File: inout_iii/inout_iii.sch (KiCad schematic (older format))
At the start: 1 part, among them P1 DIN_41612_128P

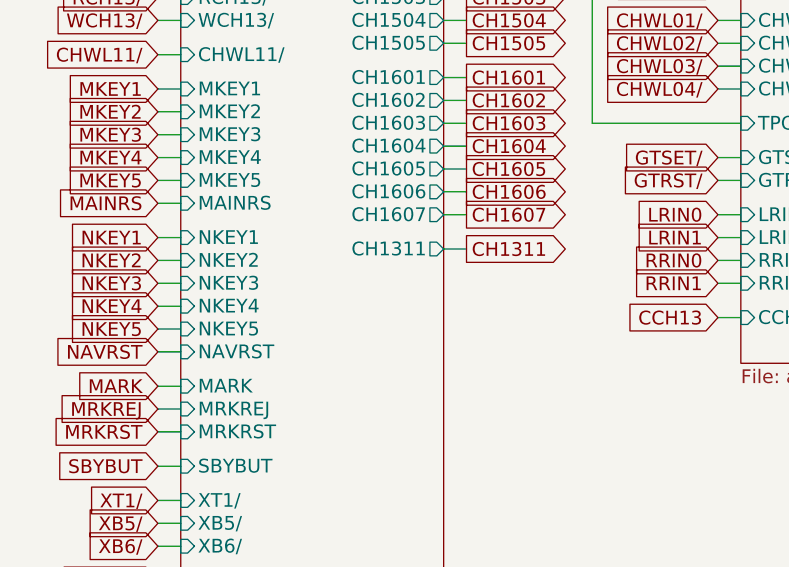
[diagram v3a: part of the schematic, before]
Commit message: Did another pass through the schematics and added in some missing gates
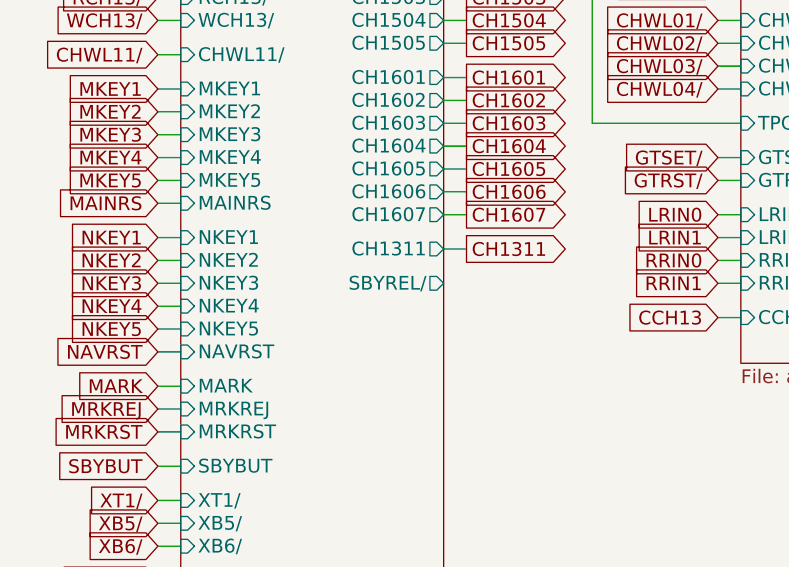
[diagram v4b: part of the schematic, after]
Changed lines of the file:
@@
 F54 "F08B" I L 1650 1800 60
 F55 "FS09/" I L 1650 1900 60
+F56 "SBYREL/" O R 2800 3800 60
 $EndSheet
 $Comp

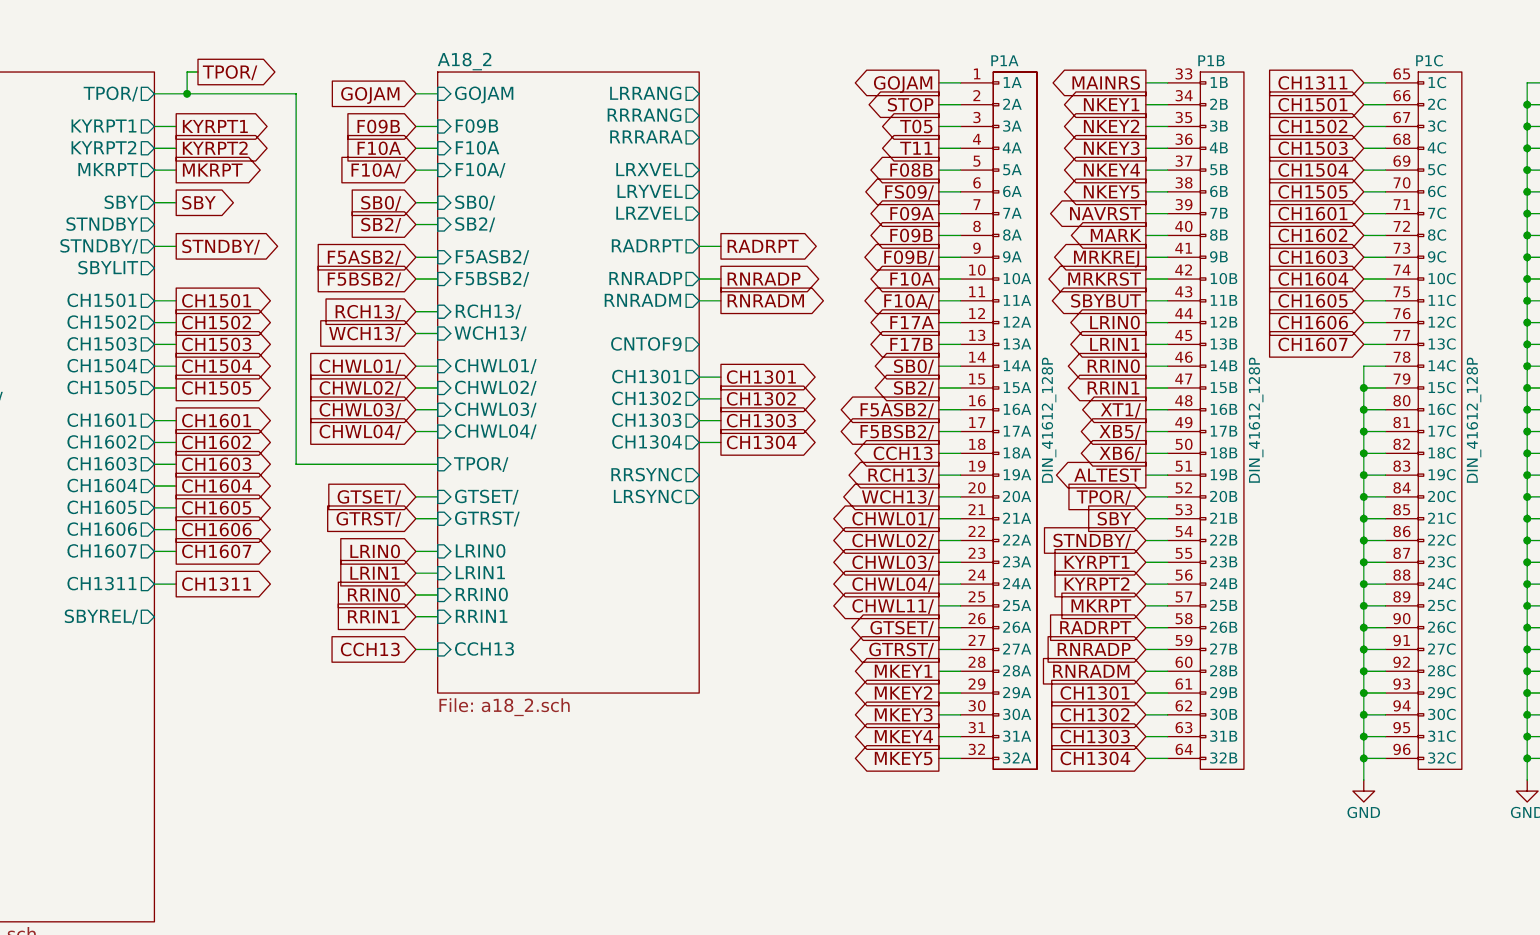
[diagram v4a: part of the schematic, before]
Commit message: Pulled out RESTRT and SBYLIT for the final two DSKY lights
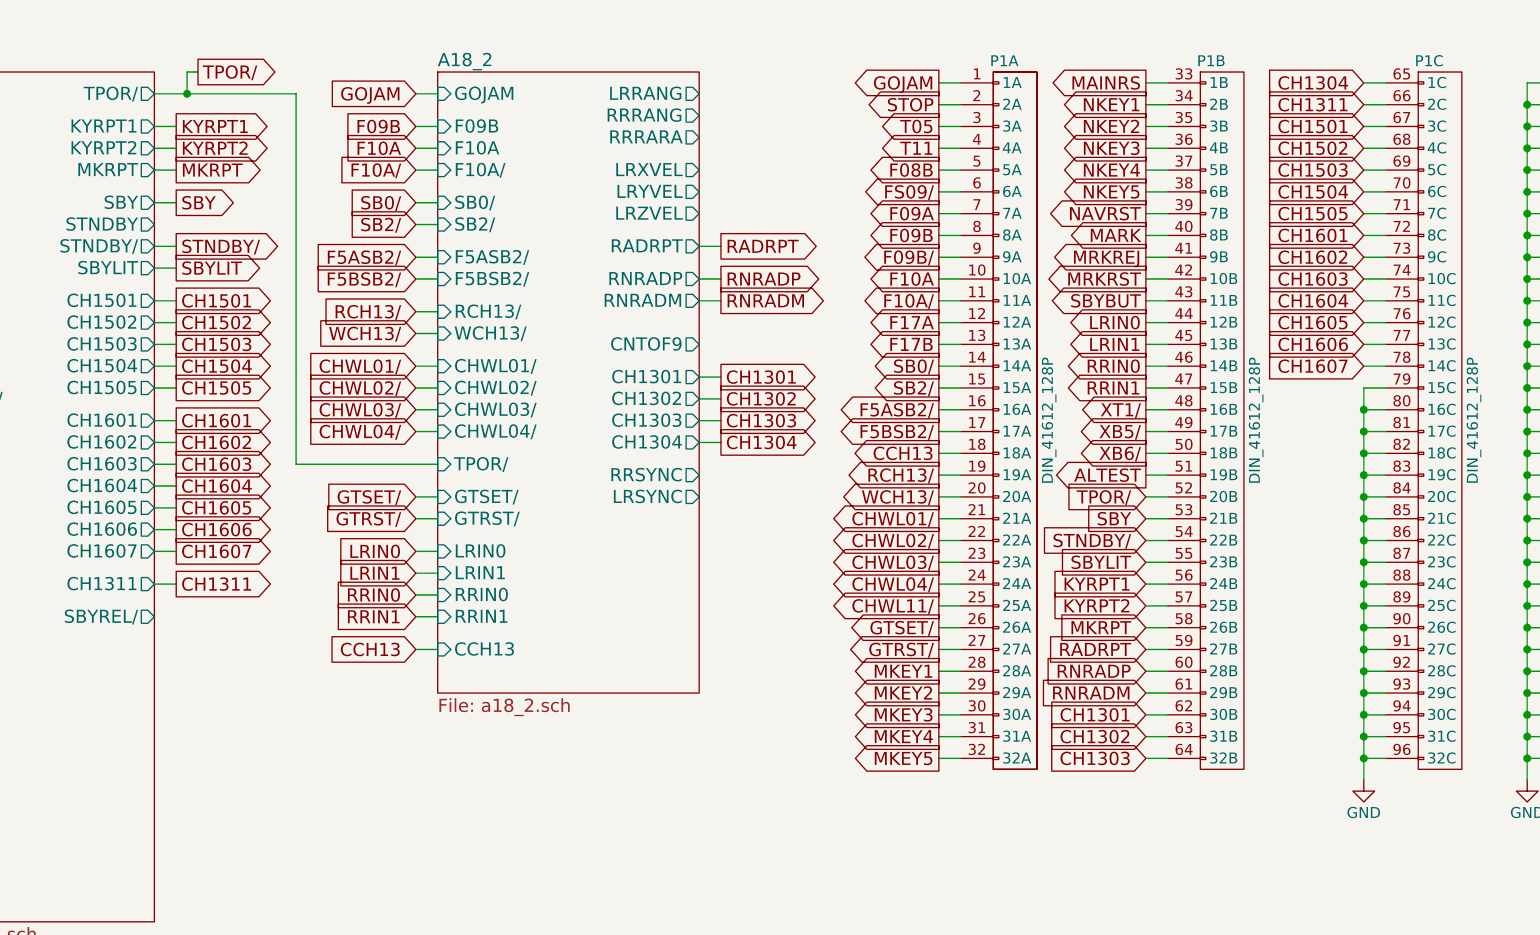
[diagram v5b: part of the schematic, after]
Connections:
- net CH1301: now also P1.62 (30B); no longer P1.61 (29B)
- net CH1302: now also P1.63 (31B); no longer P1.62 (30B)
- net CH1303: now also P1.64 (32B); no longer P1.63 (31B)
- net CH1304: now also P1.65 (1C); no longer P1.64 (32B)
- net CH1311: now also P1.66 (2C); no longer P1.65 (1C)
- net CH1501: now also P1.67 (3C); no longer P1.66 (2C)
- net CH1502: now also P1.68 (4C); no longer P1.67 (3C)
- net CH1503: now also P1.69 (5C); no longer P1.68 (4C)
- net CH1504: now also P1.70 (6C); no longer P1.69 (5C)
- net CH1505: now also P1.71 (7C); no longer P1.70 (6C)
- net CH1601: now also P1.72 (8C); no longer P1.71 (7C)
- net CH1602: now also P1.73 (9C); no longer P1.72 (8C)
- net CH1603: now also P1.74 (10C); no longer P1.73 (9C)
- net CH1604: now also P1.75 (11C); no longer P1.74 (10C)
- net CH1605: now also P1.76 (12C); no longer P1.75 (11C)
- net CH1606: now also P1.77 (13C); no longer P1.76 (12C)
- net CH1607: now also P1.78 (14C); no longer P1.77 (13C)
- net GND: no longer P1.78 (14C)
- net KYRPT1: now also P1.56 (24B); no longer P1.55 (23B)
- net KYRPT2: now also P1.57 (25B); no longer P1.56 (24B)
- net MKRPT: now also P1.58 (26B); no longer P1.57 (25B)
- net RADRPT: now also P1.59 (27B); no longer P1.58 (26B)
- net RNRADM: now also P1.61 (29B); no longer P1.60 (28B)
- net RNRADP: now also P1.60 (28B); no longer P1.59 (27B)
- new net SBYLIT: P1.55 (23B)
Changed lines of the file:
@@
 Text GLabel 2900 1750 2    60   Output ~ 0
 MKRPT
-Text GLabel 7350 3550 0    60   Input ~ 0
+Text GLabel 7350 3650 0    60   Input ~ 0
 KYRPT1
-Text GLabel 7350 3650 0    60   Input ~ 0
+Text GLabel 7350 3750 0    60   Input ~ 0
 KYRPT2
-Text GLabel 7350 3750 0    60   Input ~ 0
+Text GLabel 7350 3850 0    60   Input ~ 0
 MKRPT
 Text GLabel 2900 1900 2    60   Output ~ 0
@@
 Text GLabel 5400 2350 2    60   Output ~ 0
 RNRADM
-Text GLabel 7350 3850 0    60   Input ~ 0
+Text GLabel 7350 3950 0    60   Input ~ 0
 RADRPT
-Text GLabel 7350 3950 0    60   Input ~ 0
+Text GLabel 7350 4050 0    60   Input ~ 0
 RNRADP
-Text GLabel 7350 4050 0    60   Input ~ 0
+Text GLabel 7350 4150 0    60   Input ~ 0
 RNRADM
 Text GLabel 5400 2700 2    60   Output ~ 0
@@
 Text GLabel 2900 3650 2    60   Output ~ 0
 CH1311
-Text GLabel 7350 4150 0    60   Input ~ 0
+Text GLabel 7350 4250 0    60   Input ~ 0
 CH1301
-Text GLabel 7350 4250 0    60   Input ~ 0
+Text GLabel 7350 4350 0    60   Input ~ 0
 CH1302
-Text GLabel 7350 4350 0    60   Input ~ 0
+Text GLabel 7350 4450 0    60   Input ~ 0
 CH1303
-Text GLabel 7350 4450 0    60   Input ~ 0
+Text GLabel 8350 1350 0    60   Input ~ 0
 CH1304
-Text GLabel 8350 1350 0    60   Input ~ 0
+Text GLabel 8350 1450 0    60   Input ~ 0
 CH1311
 Text GLabel 2900 2350 2    60   Output ~ 0
@@
 Text GLabel 2900 2650 2    60   Output ~ 0
 CH1504
-Text GLabel 8350 1450 0    60   Input ~ 0
+Text GLabel 8350 1550 0    60   Input ~ 0
 CH1501
-Text GLabel 8350 1550 0    60   Input ~ 0
+Text GLabel 8350 1650 0    60   Input ~ 0
 CH1502
-Text GLabel 8350 1650 0    60   Input ~ 0
+Text GLabel 8350 1750 0    60   Input ~ 0
 CH1503
-Text GLabel 8350 1750 0    60   Input ~ 0
+Text GLabel 8350 1850 0    60   Input ~ 0
 CH1504
 Text GLabel 2900 2100 2    60   Output ~ 0
@@
 Text GLabel 2900 2750 2    60   Output ~ 0
 CH1505
-Text GLabel 8350 1850 0    60   Input ~ 0
+Text GLabel 8350 1950 0    60   Input ~ 0
 CH1505
 Text GLabel 2900 2900 2    60   Output ~ 0
@@
 Text GLabel 2900 3500 2    60   Output ~ 0
 CH1607
-Text GLabel 8350 1950 0    60   Input ~ 0
+Text GLabel 8350 2050 0    60   Input ~ 0
 CH1601
-Text GLabel 8350 2050 0    60   Input ~ 0
+Text GLabel 8350 2150 0    60   Input ~ 0
 CH1602
-Text GLabel 8350 2150 0    60   Input ~ 0
+Text GLabel 8350 2250 0    60   Input ~ 0
 CH1603
-Text GLabel 8350 2250 0    60   Input ~ 0
+Text GLabel 8350 2350 0    60   Input ~ 0
 CH1604
-Text GLabel 8350 2350 0    60   Input ~ 0
+Text GLabel 8350 2450 0    60   Input ~ 0
 CH1605
-Text GLabel 8350 2450 0    60   Input ~ 0
+Text GLabel 8350 2550 0    60   Input ~ 0
 CH1606
-Text GLabel 8350 2550 0    60   Input ~ 0
+Text GLabel 8350 2650 0    60   Input ~ 0
 CH1607
 Text GLabel 4000 3950 0    60   Input ~ 0
@@
 	2800 1750 2900 1750
 Wire Wire Line
-	7450 3550 7350 3550
-Wire Wire Line
 	7450 3650 7350 3650
 Wire Wire Line
 	7450 3750 7350 3750
 Wire Wire Line
+	7450 3850 7350 3850
+Wire Wire Line
 	2800 1900 2900 1900
 Wire Wire Line
@@
 	5300 2350 5400 2350
 Wire Wire Line
-	7450 3850 7350 3850
-Wire Wire Line
 	7450 3950 7350 3950
 Wire Wire Line
 	7450 4050 7350 4050
 Wire Wire Line
+	7450 4150 7350 4150
+Wire Wire Line
 	5300 2700 5400 2700
 Wire Wire Line
@@
 	2800 3650 2900 3650
 Wire Wire Line
-	7450 4150 7350 4150
-Wire Wire Line
 	7450 4250 7350 4250
 Wire Wire Line
@@
 	8450 1350 8350 1350
 Wire Wire Line
+	8450 1450 8350 1450
+Wire Wire Line
 	2800 2350 2900 2350
 Wire Wire Line
@@
 	2800 2650 2900 2650
 Wire Wire Line
-	8450 1450 8350 1450
-Wire Wire Line
 	8450 1550 8350 1550
 Wire Wire Line
@@
 Wire Wire Line
 	8450 1750 8350 1750
+Wire Wire Line
+	8450 1850 8350 1850
 Wire Wire Line
 	2800 2100 2900 2100
@@
 	2800 2750 2900 2750
 Wire Wire Line
-	8450 1850 8350 1850
+	8450 1950 8350 1950
 Wire Wire Line
 	2800 2900 2900 2900
@@
 	2800 3500 2900 3500
 Wire Wire Line
-	8450 1950 8350 1950
-Wire Wire Line
 	8450 2050 8350 2050
 Wire Wire Line
@@
 	8450 2550 8350 2550
 Wire Wire Line
+	8450 2650 8350 2650
+Wire Wire Line
 	4100 3950 4000 3950
-Connection ~ 8350 2750
-Wire Wire Line
-	8350 2650 8350 4550
-Wire Wire Line
-	8350 2650 8450 2650
+Text GLabel 2900 2200 2    60   Output ~ 0
+SBYLIT
+Wire Wire Line
+	2800 2200 2900 2200
+Text GLabel 7350 3550 0    60   Input ~ 0
+SBYLIT
+Wire Wire Line
+	7450 3550 7350 3550
+Wire Wire Line
+	8350 2750 8350 4550
 $EndSCHEMATC

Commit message: Updated Inout III for the new power nets. Conveniently, only the standby-controlling stuff is on standby power
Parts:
- added U18001, U18003, U18004, U18005, U18009, U18011, U18012, U18014, U18015, U18016, U18018, U18026, U18027, U18030, U18032, U18033, U18034, U18035, U18036, U18038, U18040, U18042, U18044, U18048, U18051, U18119, U18121, U18122, U18124: 74HC02, symbol 74HC02
- added U18002, U18008, U18013, U18025, U18031, U18050, U18053, U18120, U18154: 74HC04, symbol 74HC04
- added U18006, U18017, U18023, U18029, U18037, U18041, U18045, U18046, U18047, U18049, U18052, U18155: 74HC27, symbol 74HC27
- added U18007: 74LVC07, symbol 74LVC07
- added U18010, U18028, U18039, U18043: 74HC4002, symbol 74HC4002
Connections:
- net labels added: +4VDC, +4VSW
- net labels removed: VCC
- wire segments 282 -> 299

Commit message: Broke out SBYREL/ for +4VSW switching
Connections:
- net labels added: SBYREL/
- wire segments 299 -> 300
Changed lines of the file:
@@
 LIBS:contrib
 LIBS:valves
-LIBS:inout_iii-cache
 EELAYER 25 0
 EELAYER END
@@
 Text GLabel 2900 1750 2    60   Output ~ 0
 MKRPT
-Text GLabel 7350 3650 0    60   Input ~ 0
+Text GLabel 7350 3750 0    60   Input ~ 0
 KYRPT1
-Text GLabel 7350 3750 0    60   Input ~ 0
+Text GLabel 7350 3850 0    60   Input ~ 0
 KYRPT2
-Text GLabel 7350 3850 0    60   Input ~ 0
+Text GLabel 7350 3950 0    60   Input ~ 0
 MKRPT
 Text GLabel 2900 1900 2    60   Output ~ 0
@@
 Text GLabel 5400 2350 2    60   Output ~ 0
 RNRADM
-Text GLabel 7350 3950 0    60   Input ~ 0
+Text GLabel 7350 4050 0    60   Input ~ 0
 RADRPT
-Text GLabel 7350 4050 0    60   Input ~ 0
+Text GLabel 7350 4150 0    60   Input ~ 0
 RNRADP
-Text GLabel 7350 4150 0    60   Input ~ 0
+Text GLabel 7350 4250 0    60   Input ~ 0
 RNRADM
 Text GLabel 5400 2700 2    60   Output ~ 0
@@
 Text GLabel 2900 3650 2    60   Output ~ 0
 CH1311
-Text GLabel 7350 4250 0    60   Input ~ 0
+Text GLabel 7350 4350 0    60   Input ~ 0
 CH1301
-Text GLabel 7350 4350 0    60   Input ~ 0
+Text GLabel 7350 4450 0    60   Input ~ 0
 CH1302
-Text GLabel 7350 4450 0    60   Input ~ 0
+Text GLabel 8350 1350 0    60   Input ~ 0
 CH1303
-Text GLabel 8350 1350 0    60   Input ~ 0
+Text GLabel 8350 1450 0    60   Input ~ 0
 CH1304
-Text GLabel 8350 1450 0    60   Input ~ 0
+Text GLabel 8350 1550 0    60   Input ~ 0
 CH1311
 Text GLabel 2900 2350 2    60   Output ~ 0
@@
 Text GLabel 2900 2650 2    60   Output ~ 0
 CH1504
-Text GLabel 8350 1550 0    60   Input ~ 0
+Text GLabel 8350 1650 0    60   Input ~ 0
 CH1501
-Text GLabel 8350 1650 0    60   Input ~ 0
+Text GLabel 8350 1750 0    60   Input ~ 0
 CH1502
-Text GLabel 8350 1750 0    60   Input ~ 0
+Text GLabel 8350 1850 0    60   Input ~ 0
 CH1503
-Text GLabel 8350 1850 0    60   Input ~ 0
+Text GLabel 8350 1950 0    60   Input ~ 0
 CH1504
 Text GLabel 2900 2100 2    60   Output ~ 0
@@
 Text GLabel 2900 2750 2    60   Output ~ 0
 CH1505
-Text GLabel 8350 1950 0    60   Input ~ 0
+Text GLabel 8350 2050 0    60   Input ~ 0
 CH1505
 Text GLabel 2900 2900 2    60   Output ~ 0
@@
 Text GLabel 2900 3500 2    60   Output ~ 0
 CH1607
-Text GLabel 8350 2050 0    60   Input ~ 0
+Text GLabel 8350 2150 0    60   Input ~ 0
 CH1601
-Text GLabel 8350 2150 0    60   Input ~ 0
+Text GLabel 8350 2250 0    60   Input ~ 0
 CH1602
-Text GLabel 8350 2250 0    60   Input ~ 0
+Text GLabel 8350 2350 0    60   Input ~ 0
 CH1603
-Text GLabel 8350 2350 0    60   Input ~ 0
+Text GLabel 8350 2450 0    60   Input ~ 0
 CH1604
-Text GLabel 8350 2450 0    60   Input ~ 0
+Text GLabel 8350 2550 0    60   Input ~ 0
 CH1605
-Text GLabel 8350 2550 0    60   Input ~ 0
+Text GLabel 8350 2650 0    60   Input ~ 0
 CH1606
-Text GLabel 8350 2650 0    60   Input ~ 0
+Text GLabel 8350 2750 0    60   Input ~ 0
 CH1607
 Text GLabel 4000 3950 0    60   Input ~ 0
 CCH13
 Wire Wire Line
-	8350 2750 8450 2750
-Wire Wire Line
 	8350 2850 8450 2850
-Connection ~ 8350 2850
 Wire Wire Line
 	8350 2950 8450 2950
@@
 	2800 1750 2900 1750
 Wire Wire Line
-	7450 3650 7350 3650
-Wire Wire Line
 	7450 3750 7350 3750
 Wire Wire Line
 	7450 3850 7350 3850
 Wire Wire Line
+	7450 3950 7350 3950
+Wire Wire Line
 	2800 1900 2900 1900
 Wire Wire Line
@@
 	5300 2350 5400 2350
 Wire Wire Line
-	7450 3950 7350 3950
-Wire Wire Line
 	7450 4050 7350 4050
 Wire Wire Line
 	7450 4150 7350 4150
 Wire Wire Line
+	7450 4250 7350 4250
+Wire Wire Line
 	5300 2700 5400 2700
 Wire Wire Line
@@
 	2800 3650 2900 3650
 Wire Wire Line
-	7450 4250 7350 4250
-Wire Wire Line
 	7450 4350 7350 4350
 Wire Wire Line
@@
 	8450 1450 8350 1450
 Wire Wire Line
+	8450 1550 8350 1550
+Wire Wire Line
 	2800 2350 2900 2350
 Wire Wire Line
@@
 	2800 2650 2900 2650
 Wire Wire Line
-	8450 1550 8350 1550
-Wire Wire Line
 	8450 1650 8350 1650
 Wire Wire Line
@@
 Wire Wire Line
 	8450 1850 8350 1850
+Wire Wire Line
+	8450 1950 8350 1950
 Wire Wire Line
 	2800 2100 2900 2100
@@
 	2800 2750 2900 2750
 Wire Wire Line
-	8450 1950 8350 1950
+	8450 2050 8350 2050
 Wire Wire Line
 	2800 2900 2900 2900
@@
 	2800 3500 2900 3500
 Wire Wire Line
-	8450 2050 8350 2050
-Wire Wire Line
 	8450 2150 8350 2150
 Wire Wire Line
@@
 Wire Wire Line
 	8450 2650 8350 2650
+Wire Wire Line
+	8450 2750 8350 2750
 Wire Wire Line
 	4100 3950 4000 3950
@@
 Wire Wire Line
 	7450 3550 7350 3550
-Wire Wire Line
-	8350 2750 8350 4550
 $Comp
 L +4VDC #PWR05
@@
 	8950 8950 8950 9000
 Connection ~ 8950 8950
+Text GLabel 2900 3800 2    60   Output ~ 0
+SBYREL/
+Wire Wire Line
+	2800 3800 2900 3800
+Wire Wire Line
+	8350 2850 8350 4550
+Text GLabel 7350 3650 0    60   Input ~ 0
+SBYREL/
+Wire Wire Line
+	7450 3650 7350 3650
 $EndSCHEMATC
